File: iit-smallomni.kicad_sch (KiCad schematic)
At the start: 88 parts, among them J1 Battery, J10 DC-Motor, J11 Conn_02x05_Odd_Even, J12 LiPo guard, J2 HC_SR04, J3 HC_SR04, J4 HC_SR04, J5 DC-Motor, J6 DC-Motor, J7 DC-Motor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

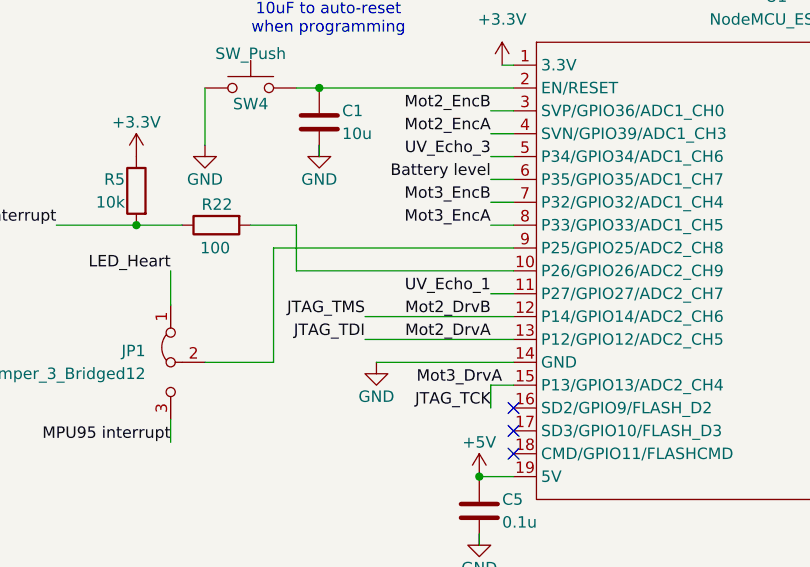
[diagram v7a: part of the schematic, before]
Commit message: Routing done, ERC & DRC errors eliminated
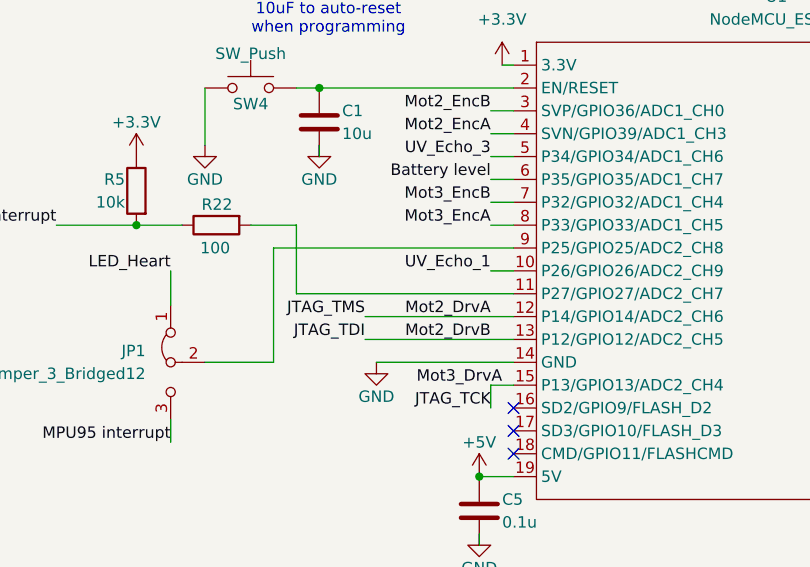
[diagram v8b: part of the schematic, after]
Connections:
- net JTAG_TDI: now also U6.1 (IN1); no longer U6.2 (IN2)
- net JTAG_TMS: now also U6.2 (IN2); no longer U6.1 (IN1)
- net UV_Echo_1: now also U1.10 (P26/GPIO26/ADC2_CH9); no longer U1.11 (P27/GPIO27/ADC2_CH7)
- net at R22.2: now also U1.11 (P27/GPIO27/ADC2_CH7); no longer U1.10 (P26/GPIO26/ADC2_CH9)
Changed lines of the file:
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@@
 	(wire
 		(pts
+			(xy 190.5 59.69) (xy 193.04 59.69)
+		)
+		(stroke
+			(width 0)
+			(type default)
+		)
+	)
+	(wire
+		(pts
 			(xy 34.29 85.09) (xy 34.29 86.36)
 		)
@@
 	(wire
 		(pts
-			(xy 168.91 54.61) (xy 168.91 59.69)
+			(xy 168.91 54.61) (xy 168.91 62.23)
 		)
 		(stroke
@@
 	(wire
 		(pts
-			(xy 168.91 59.69) (xy 193.04 59.69)
-		)
-		(stroke
-			(width 0)
-			(type default)
-		)
-	)
-	(wire
-		(pts
 			(xy 213.36 129.54) (xy 217.17 129.54)
 		)
@@
 	(wire
 		(pts
-			(xy 190.5 62.23) (xy 193.04 62.23)
+			(xy 168.91 62.23) (xy 193.04 62.23)
 		)
 		(stroke
@@
 	)
 	(label "Mot2_DrvB"
-		(at 190.5 64.77 180)
+		(at 190.5 67.31 180)
 		(fields_autoplaced yes)
 		(effects
@@
 	)
 	(label "Mot2_DrvA"
-		(at 190.5 67.31 180)
+		(at 190.5 64.77 180)
 		(fields_autoplaced yes)
 		(effects
@@
 	)
 	(label "UV_Echo_1"
-		(at 190.5 62.23 180)
+		(at 190.5 59.69 180)
 		(fields_autoplaced yes)
 		(effects
